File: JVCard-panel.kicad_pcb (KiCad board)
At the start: 2 copper layers, 92.5 x 154.5 mm, 8 parts

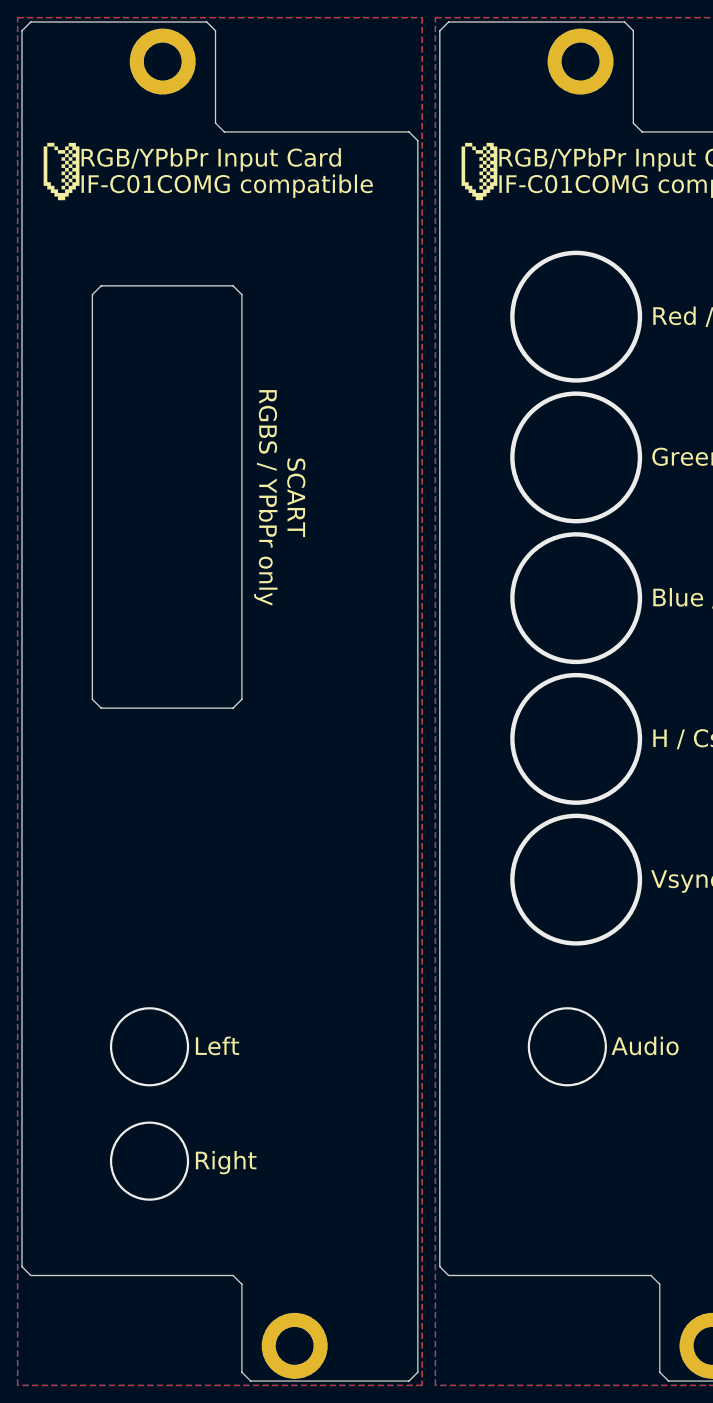
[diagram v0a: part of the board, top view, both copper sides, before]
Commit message: migrate to kicad 6, panel covering extended a little
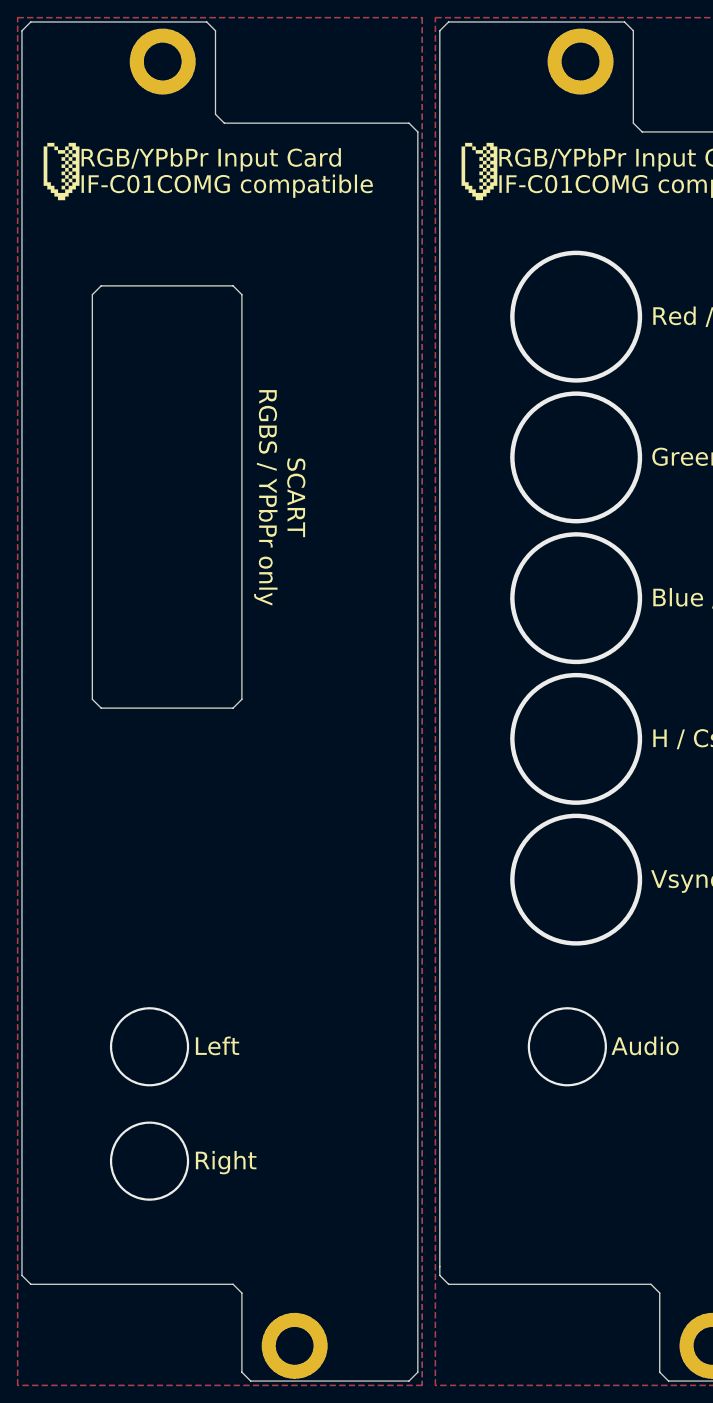
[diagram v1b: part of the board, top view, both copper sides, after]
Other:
- outline, holes or cut-outs redrawn
- net class Default removed

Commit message: new gerbers for BNC and SCART hole plates
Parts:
- moved G*** 200.9 mm to (83.1, 44.8)
- moved G*** 200.9 mm to (35.6, 44.8)
- moved G*** 200.9 mm to (68.6, 165.8)
- moved G*** 200.9 mm to (117.1, 165.8)
- moved REF** 200.9 mm to (94.6, 32.2)
- moved REF** 200.9 mm to (109.6, 178.2)
- moved REF** 200.9 mm to (47.1, 32.2)
- moved REF** 200.9 mm to (62.1, 178.2)
